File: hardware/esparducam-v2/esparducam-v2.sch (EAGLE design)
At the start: 30 parts, among them J1 FTDI_DEVICE, J2 JST_ZH_3PIN, Q2 MOSFET-PCHANNEL, U1 NCP1117, U2 SPI flash

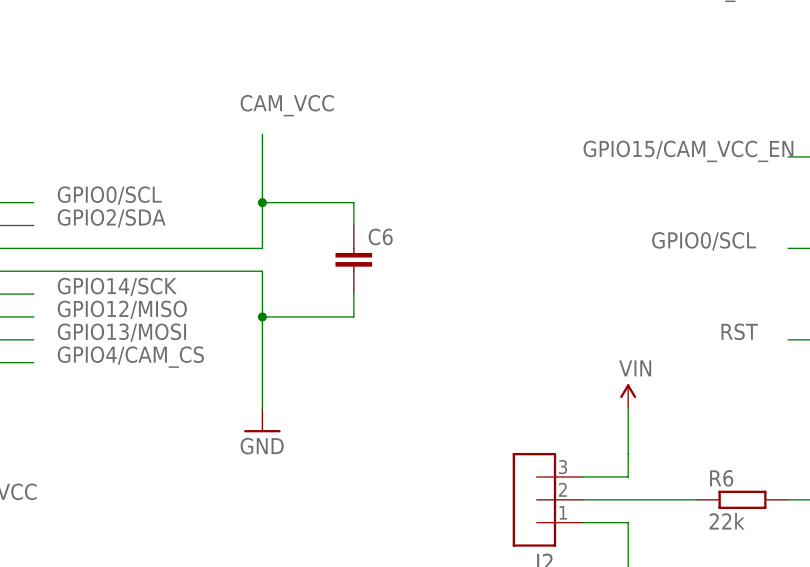
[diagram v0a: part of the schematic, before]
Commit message: Updated value for C6
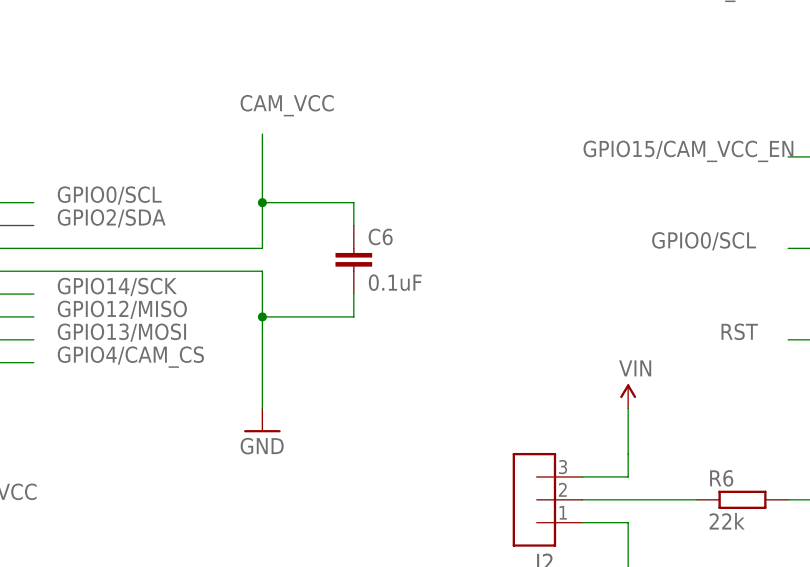
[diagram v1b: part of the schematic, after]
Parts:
- C6: value (none) -> 0.1uF
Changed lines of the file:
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@@
 <part name="C4" library="SparkFun-Capacitors" deviceset="CAP" device="0603-CAP" value="10uF"/>
 <part name="C5" library="SparkFun-Capacitors" deviceset="CAP" device="0603-CAP" value="0.1uF"/>
-<part name="C6" library="SparkFun-Capacitors" deviceset="CAP" device="0603-CAP"/>
+<part name="C6" library="SparkFun-Capacitors" deviceset="CAP" device="0603-CAP" value="0.1uF"/>
 <part name="GND7" library="SparkFun-Aesthetics" deviceset="GND" device=""/>
 <part name="SUPPLY12" library="SparkFun-Aesthetics" deviceset="VCC" device=""/>
